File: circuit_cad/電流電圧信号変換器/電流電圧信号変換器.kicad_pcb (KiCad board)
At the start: 2 copper layers, 47 x 72 mm, 11 parts, among them J1 sensor(M12), J2 +Vin, J3 -Vin, J4 ADconverter, J5 GND

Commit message: 文字入れまで完成
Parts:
- AD converter: renamed from J4
- renumbered J2 to +Vin, J3 to -Vin, J5 to GNDA, J1 to sensor
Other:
- board text added: "+(2-w) -(3-w) I_in"
- board text added: "+(3-w)"
- board text added: "-(2-w) I_out"
- board text added: "2線式:抵抗設置 3線式：R1端子間ショート 電流読取：何も接続しない"
- board text added: "2線式or電流読取:FREE 3線式:抵抗設置"
- board text added: "4-20mA → 2-10V(500ohm) 1-5V(250ohm)"
- board text added: "Created by YOSHIDA Yuji (2024/2)"
- board text added: "GNDA"
- board text added: "I (3-w)"
- board text added: "JLCJLCJLCJLC"
- board text added: "return"
- board text added: "supply"
- board text added: "灰５"
- board text added: "白２"
- board text added: "茶１"
- board text added: "電流電圧変換基板"
- board text added: "青３"
- board text added: "黒４"
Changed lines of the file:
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@@
     (property "ki_keywords" "connector")
     (attr through_hole)
-    (fp_text reference "J3" (at 3 -3.5 unlocked) (layer "F.SilkS")
+    (fp_text reference "-Vin" (at 3 -3.5 unlocked) (layer "F.SilkS")
         (effects (font (size 1 1) (thickness 0.1)))
     )
@@
     (property "ki_keywords" "connector")
     (attr through_hole)
-    (fp_text reference "J4" (at 9 -3.5 -90 unlocked) (layer "F.SilkS")
+    (fp_text reference "AD converter" (at 6.96 -3.5 -90 unlocked) (layer "F.SilkS")
         (effects (font (size 1 1) (thickness 0.1)))
     )
@@
     (property "ki_keywords" "connector")
     (attr through_hole)
-    (fp_text reference "J2" (at 3 -3.5 unlocked) (layer "F.SilkS")
+    (fp_text reference "+Vin" (at 3 -3.5 unlocked) (layer "F.SilkS")
         (effects (font (size 1 1) (thickness 0.1)))
     )
@@
     (property "ki_keywords" "connector")
     (attr through_hole)
-    (fp_text reference "J1" (at 10.5 -3.5 90 unlocked) (layer "F.SilkS")
+    (fp_text reference "sensor" (at 10.5 -3.5 90 unlocked) (layer "F.SilkS")
         (effects (font (size 1 1) (thickness 0.1)))
     )
@@
     (property "ki_keywords" "connector")
     (attr through_hole)
-    (fp_text reference "J5" (at 3 -3.5 -90 unlocked) (layer "F.SilkS")
+    (fp_text reference "GNDA" (at 1.75 -3.5 -90 unlocked) (layer "F.SilkS")
         (effects (font (size 1 1) (thickness 0.1)))
     )
@@
       (net 4 "GNDA"))
   )
+  (gr_line (start 66.675 63.5) (end 64.135 63.5)
+    (stroke (width 0.15) (type default)) (layer "B.SilkS"))
+  (gr_line (start 68.58 66.675) (end 68.58 65.405)
+    (stroke (width 0.15) (type default)) (layer "B.SilkS"))
+  (gr_line (start 69.85 66.675) (end 68.58 66.675)
+    (stroke (width 0.15) (type default)) (layer "B.SilkS"))
+  (gr_line (start 72.39 92.075) (end 85.09 92.075)
+    (stroke (width 0.15) (type default)) (layer "B.SilkS"))
+  (gr_line (start 53.975 106.045) (end 53.975 115.57)
+    (stroke (width 0.15) (type default)) (layer "B.SilkS"))
+  (gr_line (start 81.915 113.03) (end 83.185 113.03)
+    (stroke (width 0.15) (type default)) (layer "B.SilkS"))
+  (gr_line (start 87.63 99.695) (end 87.63 110.49)
+    (stroke (width 0.15) (type default)) (layer "B.SilkS"))
+  (gr_line (start 86.36 77.47) (end 83.82 77.47)
+    (stroke (width 0.15) (type default)) (layer "B.SilkS"))
+  (gr_line (start 62.23 71.12) (end 66.675 71.12)
+    (stroke (width 0.15) (type default)) (layer "B.SilkS"))
+  (gr_line (start 56.515 52.705) (end 90.805 52.705)
+    (stroke (width 0.15) (type default)) (layer "B.SilkS"))
+  (gr_line (start 94.615 55.88) (end 94.615 115.57)
+    (stroke (width 0.15) (type default)) (layer "B.SilkS"))
+  (gr_line (start 64.135 66.675) (end 61.595 66.675)
+    (stroke (width 0.15) (type default)) (layer "B.SilkS"))
+  (gr_line (start 65.405 76.2) (end 62.23 76.2)
+    (stroke (width 0.15) (type default)) (layer "B.SilkS"))
+  (gr_line (start 68.58 83.82) (end 68.58 111.125)
+    (stroke (width 0.15) (type default)) (layer "B.SilkS"))
+  (gr_line (start 59.69 97.155) (end 59.69 98.425)
+    (stroke (width 0.15) (type default)) (layer "B.SilkS"))
+  (gr_line (start 83.82 77.47) (end 83.82 82.55)
+    (stroke (width 0.15) (type default)) (layer "B.SilkS"))
+  (gr_line (start 72.39 88.9) (end 72.39 92.075)
+    (stroke (width 0.15) (type default)) (layer "B.SilkS"))
+  (gr_line (start 55.88 119.38) (end 90.805 119.38)
+    (stroke (width 0.15) (type default)) (layer "B.SilkS"))
+  (gr_line (start 68.58 72.39) (end 68.58 80.645)
+    (stroke (width 0.15) (type default)) (layer "B.SilkS"))
+  (gr_line (start 59.69 102.235) (end 59.69 106.045)
+    (stroke (width 0.15) (type default)) (layer "B.SilkS"))
+  (gr_line (start 80.01 66.675) (end 76.2 66.675)
+    (stroke (width 0.15) (type default)) (layer "B.SilkS"))
+  (gr_line (start 87.63 110.49) (end 86.36 111.76)
+    (stroke (width 0.15) (type default)) (layer "B.SilkS"))
+  (gr_line (start 83.82 77.47) (end 83.82 52.705)
+    (stroke (width 0.15) (type default)) (layer "B.SilkS"))
+  (gr_line (start 64.135 63.5) (end 64.135 66.675)
+    (stroke (width 0.15) (type default)) (layer "B.SilkS"))
+  (gr_line (start 65.405 113.03) (end 66.675 113.03)
+    (stroke (width 0.15) (type default)) (layer "B.SilkS"))
+  (gr_line (start 59.69 106.045) (end 53.975 106.045)
+    (stroke (width 0.15) (type default)) (layer "B.SilkS"))
+  (gr_line (start 65.405 87.63) (end 65.405 76.2)
+    (stroke (width 0.15) (type default)) (layer "B.SilkS"))
+  (gr_line (start 59.69 83.185) (end 59.69 93.345)
+    (stroke (width 0.15) (type default)) (layer "B.SilkS"))
+  (gr_line (start 80.01 86.36) (end 80.01 85.09)
+    (stroke (width 0.15) (type default)) (layer "B.SilkS"))
+  (gr_line (start 71.12 87.63) (end 65.405 87.63)
+    (stroke (width 0.15) (type default)) (layer "B.SilkS"))
+  (gr_line (start 81.28 87.63) (end 85.725 87.63)
+    (stroke (width 0.15) (type default)) (layer "B.SilkS"))
+  (gr_line (start 83.82 82.55) (end 85.09 82.55)
+    (stroke (width 0.15) (type default)) (layer "B.SilkS"))
+  (gr_line (start 80.01 81.28) (end 80.01 66.675)
+    (stroke (width 0.15) (type default)) (layer "B.SilkS"))
   (gr_rect (start 50 50) (end 97 122)
     (stroke (width 0.1) (type default)) (fill none) (layer "Edge.Cuts"))
+  (gr_text "return" (at 88.9 85.725) (layer "B.SilkS")
+    (effects (font (size 0.8 0.8) (thickness 0.15)) (justify left bottom mirror))
+  )
+  (gr_text "GNDA" (at 88.9 80.645) (layer "B.SilkS")
+    (effects (font (size 0.8 0.8) (thickness 0.15)) (justify left bottom mirror))
+  )
+  (gr_text "2線式:抵抗設置\n3線式：R1端子間ショート\n電流読取：何も接続しない" (at 75 60 90) (layer "B.SilkS")
+    (effects (font (size 1 1) (thickness 0.15)) (justify left bottom mirror))
+  )
+  (gr_text "GNDA" (at 57.785 95.885) (layer "B.SilkS")
+    (effects (font (size 1 1) (thickness 0.15)) (justify left bottom mirror))
+  )
+  (gr_text "-(2-w)\n I_out" (at 57.785 72.39) (layer "B.SilkS")
+    (effects (font (size 1 1) (thickness 0.15)) (justify left bottom mirror))
+  )
+  (gr_text "白２" (at 92.71 93.98) (layer "B.SilkS")
+    (effects (font (size 1 1) (thickness 0.15)) (justify left bottom mirror))
+  )
+  (gr_text "+(3-w)" (at 57.785 76.835) (layer "B.SilkS")
+    (effects (font (size 1 1) (thickness 0.15)) (justify left bottom mirror))
+  )
+  (gr_text "2線式or電流読取:FREE\n3線式:抵抗設置" (at 82.55 84.455) (layer "B.SilkS")
+    (effects (font (size 1 1) (thickness 0.15)) (justify left bottom mirror))
+  )
+  (gr_text "GNDA" (at 57.785 81.915) (layer "B.SilkS")
+    (effects (font (size 1 1) (thickness 0.15)) (justify left bottom mirror))
+  )
+  (gr_text "青３" (at 92.71 88.9) (layer "B.SilkS")
+    (effects (font (size 1 1) (thickness 0.15)) (justify left bottom mirror))
+  )
+  (gr_text "supply" (at 88.9 95.885) (layer "B.SilkS")
+    (effects (font (size 0.8 0.8) (thickness 0.15)) (justify left bottom mirror))
+  )
+  (gr_text "黒４" (at 92.71 83.82) (layer "B.SilkS")
+    (effects (font (size 1 1) (thickness 0.15)) (justify left bottom mirror))
+  )
+  (gr_text "GNDA" (at 57.785 100.965) (layer "B.SilkS")
+    (effects (font (size 1 1) (thickness 0.15)) (justify left bottom mirror))
+  )
+  (gr_text "茶１" (at 92.71 99.06) (layer "B.SilkS")
+    (effects (font (size 1 1) (thickness 0.15)) (justify left bottom mirror))
+  )
+  (gr_text "GNDA" (at 88.9 75.565) (layer "B.SilkS")
+    (effects (font (size 0.8 0.8) (thickness 0.15)) (justify left bottom mirror))
+  )
+  (gr_text "+(2-w)\n-(3-w)\n I_in" (at 57.785 67.31) (layer "B.SilkS")
+    (effects (font (size 1 1) (thickness 0.15)) (justify left bottom mirror))
+  )
+  (gr_text "Created by YOSHIDA Yuji (2024/2)" (at 89.535 118.745) (layer "B.SilkS")
+    (effects (font (size 1.4 1.2) (thickness 0.15)) (justify left bottom mirror))
+  )
+  (gr_text "I (3-w)" (at 88.9 90.805) (layer "B.SilkS")
+    (effects (font (size 0.8 0.8) (thickness 0.15)) (justify left bottom mirror))
+  )
+  (gr_text "灰５" (at 92.71 78.74) (layer "B.SilkS")
+    (effects (font (size 1 1) (thickness 0.15)) (justify left bottom mirror))
+  )
+  (gr_text "JLCJLCJLCJLC" (at 93 93 90) (layer "F.SilkS")
+    (effects (font (size 1 1) (thickness 0.15)) (justify left bottom))
+  )
+  (gr_text "電流電圧変換基板" (at 60 54.61) (layer "F.SilkS")
+    (effects (font (size 1.6 1.4) (thickness 0.15)) (justify left bottom))
+  )
+  (gr_text "4-20mA → 2-10V(500ohm)\n1-5V(250ohm)" (at 81.915 59.055) (layer "F.SilkS")
+    (effects (font (size 1.2 1) (thickness 0.15)) (justify right bottom))
+  )
   (segment (start 80.01 113.03) (end 85.09 113.03) (width 6) (layer "F.Cu") (net 1))
   (segment (start 87.63 110.49) (end 85.09 113.03) (width 2) (layer "B.Cu") (net 1))

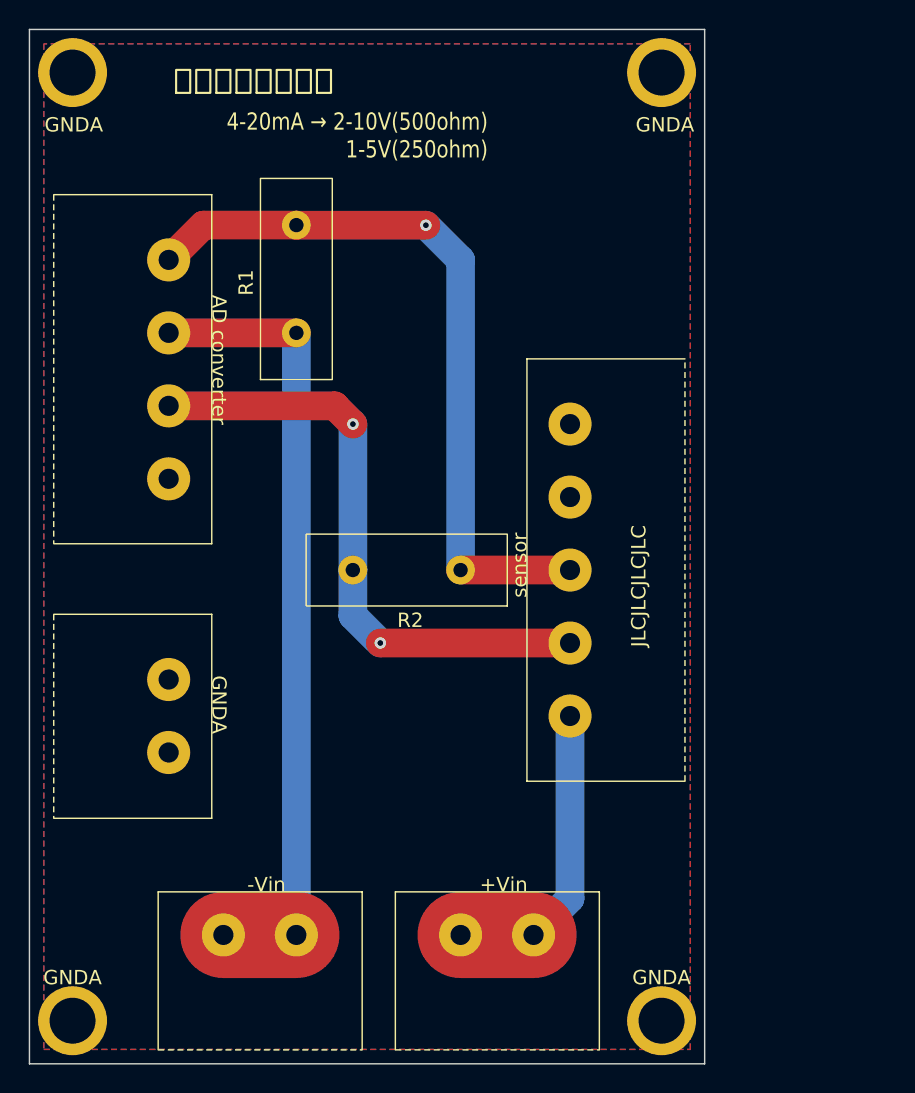
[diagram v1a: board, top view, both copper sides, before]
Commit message: 電源回路作成
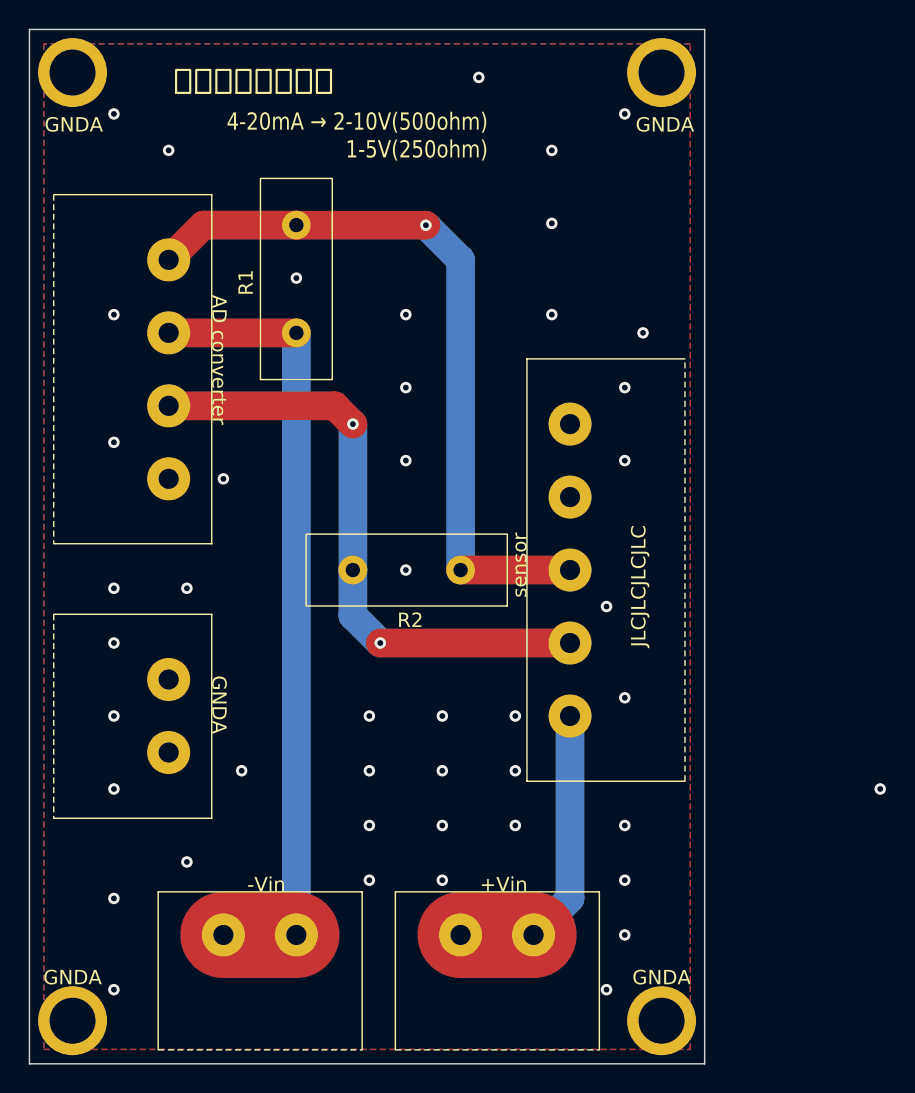
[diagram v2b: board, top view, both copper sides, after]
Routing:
- net GNDA: vias 0 -> 44
- net (no net): vias 0 -> 1
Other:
- board text added: "2-3:V-,I-"
- board text added: "2-w or I :FREE 3-w:抵抗設置"
- board text added: "2-w:2線式センサ 3-w:3線式センサ I :電流直接出力"
- board text added: "2-w:V+,I+ 3-w:V-,I-"
- board text added: "2-w:抵抗設置 3-w：R1端子間ショート I：何も接続しない"
- board text added: "3-w:V+,I+"
- board text removed: "+(2-w) -(3-w) I_in"
- board text removed: "+(3-w)"
- board text removed: "-(2-w) I_out"
- board text removed: "2線式:抵抗設置 3線式：R1端子間ショート 電流読取：何も接続しない"
- board text removed: "2線式or電流読取:FREE 3線式:抵抗設置"
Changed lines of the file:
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@@
     (effects (font (size 0.8 0.8) (thickness 0.15)) (justify left bottom mirror))
   )
-  (gr_text "2線式:抵抗設置\n3線式：R1端子間ショート\n電流読取：何も接続しない" (at 75 60 90) (layer "B.SilkS")
+  (gr_text "2-w:抵抗設置\n3-w：R1端子間ショート\nI：何も接続しない" (at 75 60 90) (layer "B.SilkS")
     (effects (font (size 1 1) (thickness 0.15)) (justify left bottom mirror))
   )
@@
     (effects (font (size 1 1) (thickness 0.15)) (justify left bottom mirror))
   )
-  (gr_text "-(2-w)\n I_out" (at 57.785 72.39) (layer "B.SilkS")
-    (effects (font (size 1 1) (thickness 0.15)) (justify left bottom mirror))
+  (gr_text "2-3:V-,I-" (at 57.785 72.39) (layer "B.SilkS")
+    (effects (font (size 1.2 0.8) (thickness 0.15)) (justify left bottom mirror))
   )
   (gr_text "白２" (at 92.71 93.98) (layer "B.SilkS")
     (effects (font (size 1 1) (thickness 0.15)) (justify left bottom mirror))
   )
-  (gr_text "+(3-w)" (at 57.785 76.835) (layer "B.SilkS")
-    (effects (font (size 1 1) (thickness 0.15)) (justify left bottom mirror))
+  (gr_text "3-w:V+,I+" (at 57.785 76.835) (layer "B.SilkS")
+    (effects (font (size 1.2 0.8) (thickness 0.15)) (justify left bottom mirror))
   )
-  (gr_text "2線式or電流読取:FREE\n3線式:抵抗設置" (at 82.55 84.455) (layer "B.SilkS")
+  (gr_text "2-w or I :FREE\n3-w:抵抗設置" (at 82.55 84.455) (layer "B.SilkS")
     (effects (font (size 1 1) (thickness 0.15)) (justify left bottom mirror))
   )
   (gr_text "GNDA" (at 57.785 81.915) (layer "B.SilkS")
-    (effects (font (size 1 1) (thickness 0.15)) (justify left bottom mirror))
+    (effects (font (size 1.2 0.8) (thickness 0.15)) (justify left bottom mirror))
   )
   (gr_text "青３" (at 92.71 88.9) (layer "B.SilkS")
@@
     (effects (font (size 1 1) (thickness 0.15)) (justify left bottom mirror))
   )
+  (gr_text "2-w:2線式センサ\n3-w:3線式センサ\nI :電流直接出力" (at 92.71 58.42 90) (layer "B.SilkS")
+    (effects (font (size 1 1) (thickness 0.15)) (justify left bottom mirror))
+  )
   (gr_text "茶１" (at 92.71 99.06) (layer "B.SilkS")
     (effects (font (size 1 1) (thickness 0.15)) (justify left bottom mirror))
@@
     (effects (font (size 0.8 0.8) (thickness 0.15)) (justify left bottom mirror))
   )
-  (gr_text "+(2-w)\n-(3-w)\n I_in" (at 57.785 67.31) (layer "B.SilkS")
-    (effects (font (size 1 1) (thickness 0.15)) (justify left bottom mirror))
+  (gr_text "2-w:V+,I+\n3-w:V-,I-" (at 57.785 67.31) (layer "B.SilkS")
+    (effects (font (size 1.2 0.8) (thickness 0.15)) (justify left bottom mirror))
   )
   (gr_text "Created by YOSHIDA Yuji (2024/2)" (at 89.535 118.745) (layer "B.SilkS")
@@
     (effects (font (size 1.2 1) (thickness 0.15)) (justify right bottom))
   )
+  (via (at 109.22 102.87) (size 0.8) (drill 0.4) (layers "F.Cu" "B.Cu") (net 0))
   (segment (start 80.01 113.03) (end 85.09 113.03) (width 6) (layer "F.Cu") (net 1))
   (segment (start 87.63 110.49) (end 85.09 113.03) (width 2) (layer "B.Cu") (net 1))
@@
   (segment (start 80.01 66.04) (end 77.597 63.627) (width 2) (layer "B.Cu") (net 3))
   (segment (start 80.01 87.63) (end 80.01 66.04) (width 2) (layer "B.Cu") (net 3))
+  (via (at 55.88 97.79) (size 0.8) (drill 0.4) (layers "F.Cu" "B.Cu") (free) (net 4))
+  (via (at 86.36 69.85) (size 0.8) (drill 0.4) (layers "F.Cu" "B.Cu") (free) (net 4))
+  (via (at 63.5 81.28) (size 0.8) (drill 0.4) (layers "F.Cu" "B.Cu") (free) (net 4))
+  (via (at 73.66 109.22) (size 0.8) (drill 0.4) (layers "F.Cu" "B.Cu") (free) (net 4))
+  (via (at 76.2 80.01) (size 0.8) (drill 0.4) (layers "F.Cu" "B.Cu") (free) (net 4))
+  (via (at 91.44 74.93) (size 0.8) (drill 0.4) (layers "F.Cu" "B.Cu") (free) (net 4))
+  (via (at 86.36 63.5) (size 0.8) (drill 0.4) (layers "F.Cu" "B.Cu") (free) (net 4))
+  (via (at 83.82 97.79) (size 0.8) (drill 0.4) (layers "F.Cu" "B.Cu") (free) (net 4))
+  (via (at 92.71 71.12) (size 0.8) (drill 0.4) (layers "F.Cu" "B.Cu") (free) (net 4))
+  (via (at 78.74 109.22) (size 0.8) (drill 0.4) (layers "F.Cu" "B.Cu") (free) (net 4))
+  (via (at 86.36 58.42) (size 0.8) (drill 0.4) (layers "F.Cu" "B.Cu") (free) (net 4))
+  (via (at 90.17 90.17) (size 0.8) (drill 0.4) (layers "F.Cu" "B.Cu") (free) (net 4))
+  (via (at 60.96 107.95) (size 0.8) (drill 0.4) (layers "F.Cu" "B.Cu") (free) (net 4))
+  (via (at 83.82 105.41) (size 0.8) (drill 0.4) (layers "F.Cu" "B.Cu") (free) (net 4))
+  (via (at 91.44 109.22) (size 0.8) (drill 0.4) (layers "F.Cu" "B.Cu") (free) (net 4))
+  (via (at 55.88 88.9) (size 0.8) (drill 0.4) (layers "F.Cu" "B.Cu") (free) (net 4))
+  (via (at 55.88 102.87) (size 0.8) (drill 0.4) (layers "F.Cu" "B.Cu") (free) (net 4))
+  (via (at 73.66 97.79) (size 0.8) (drill 0.4) (layers "F.Cu" "B.Cu") (free) (net 4))
+  (via (at 91.44 80.01) (size 0.8) (drill 0.4) (layers "F.Cu" "B.Cu") (free) (net 4))
+  (via (at 60.96 88.9) (size 0.8) (drill 0.4) (layers "F.Cu" "B.Cu") (free) (net 4))
+  (via (at 91.44 55.88) (size 0.8) (drill 0.4) (layers "F.Cu" "B.Cu") (free) (net 4))
+  (via (at 73.66 105.41) (size 0.8) (drill 0.4) (layers "F.Cu" "B.Cu") (free) (net 4))
+  (via (at 59.69 58.42) (size 0.8) (drill 0.4) (layers "F.Cu" "B.Cu") (free) (net 4))
+  (via (at 55.88 92.71) (size 0.8) (drill 0.4) (layers "F.Cu" "B.Cu") (free) (net 4))
+  (via (at 76.2 74.93) (size 0.8) (drill 0.4) (layers "F.Cu" "B.Cu") (free) (net 4))
+  (via (at 91.44 105.41) (size 0.8) (drill 0.4) (layers "F.Cu" "B.Cu") (free) (net 4))
+  (via (at 55.88 78.74) (size 0.8) (drill 0.4) (layers "F.Cu" "B.Cu") (free) (net 4))
+  (via (at 91.44 96.52) (size 0.8) (drill 0.4) (layers "F.Cu" "B.Cu") (free) (net 4))
+  (via (at 76.2 87.63) (size 0.8) (drill 0.4) (layers "F.Cu" "B.Cu") (free) (net 4))
+  (via (at 91.44 113.03) (size 0.8) (drill 0.4) (layers "F.Cu" "B.Cu") (free) (net 4))
+  (via (at 55.88 55.88) (size 0.8) (drill 0.4) (layers "F.Cu" "B.Cu") (free) (net 4))
+  (via (at 81.28 53.34) (size 0.8) (drill 0.4) (layers "F.Cu" "B.Cu") (free) (net 4))
+  (via (at 73.66 101.6) (size 0.8) (drill 0.4) (layers "F.Cu" "B.Cu") (free) (net 4))
+  (via (at 55.88 116.84) (size 0.8) (drill 0.4) (layers "F.Cu" "B.Cu") (free) (net 4))
+  (via (at 78.74 101.6) (size 0.8) (drill 0.4) (layers "F.Cu" "B.Cu") (free) (net 4))
+  (via (at 83.82 101.6) (size 0.8) (drill 0.4) (layers "F.Cu" "B.Cu") (free) (net 4))
+  (via (at 68.58 67.31) (size 0.8) (drill 0.4) (layers "F.Cu" "B.Cu") (free) (net 4))
+  (via (at 90.17 116.84) (size 0.8) (drill 0.4) (layers "F.Cu" "B.Cu") (free) (net 4))
+  (via (at 55.88 69.85) (size 0.8) (drill 0.4) (layers "F.Cu" "B.Cu") (free) (net 4))
+  (via (at 78.74 97.79) (size 0.8) (drill 0.4) (layers "F.Cu" "B.Cu") (free) (net 4))
+  (via (at 78.74 105.41) (size 0.8) (drill 0.4) (layers "F.Cu" "B.Cu") (free) (net 4))
+  (via (at 64.77 101.6) (size 0.8) (drill 0.4) (layers "F.Cu" "B.Cu") (free) (net 4))
+  (via (at 55.88 110.49) (size 0.8) (drill 0.4) (layers "F.Cu" "B.Cu") (free) (net 4))
+  (via (at 76.2 69.85) (size 0.8) (drill 0.4) (layers "F.Cu" "B.Cu") (free) (net 4))
   (segment (start 68.58 71.12) (end 59.69 71.12) (width 2) (layer "F.Cu") (net 5))
   (segment (start 63.5 113.03) (end 68.58 113.03) (width 6) (layer "F.Cu") (net 5))
